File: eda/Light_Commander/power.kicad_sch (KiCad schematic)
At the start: 14 parts, among them J13 Eurorack_Power, Q5 Q_PMOS_GSD, Q6 Q_NMOS_GSD, U4 R-785.0-0.5, U5 AP2112K-3.3

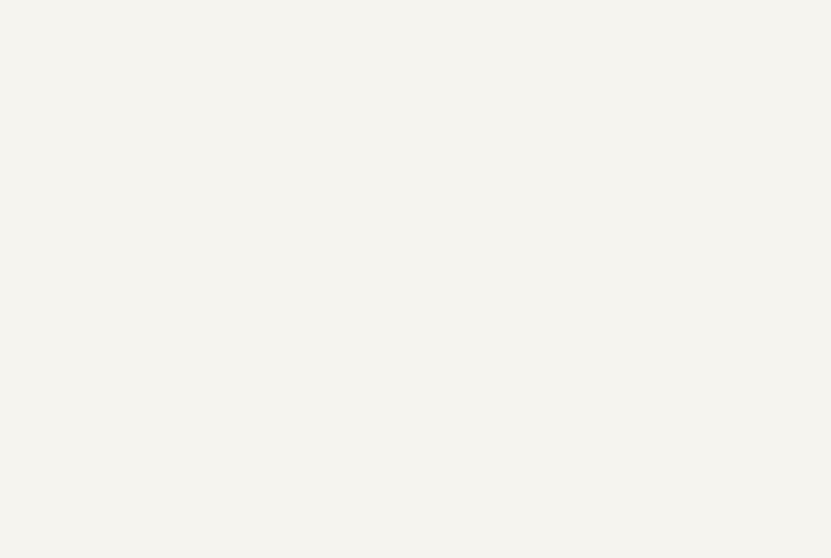
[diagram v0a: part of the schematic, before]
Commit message: Voltage ref, BOOT0, and connections on PCB
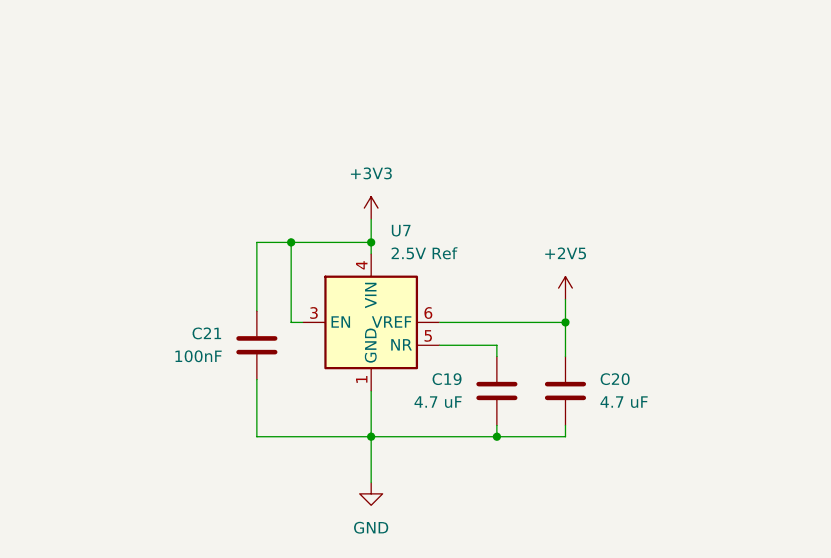
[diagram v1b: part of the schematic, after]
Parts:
- added C19, C20: 4.7 uF, Capacitor_SMD:C_0805_2012Metric, symbol Device:C
- added C21: 100nF, Capacitor_SMD:C_0805_2012Metric, symbol Device:C
- added U7: 2.5V Ref, Package_TO_SOT_SMD:SOT-23-6, symbol Reference_Voltage:REF35250QDBVR
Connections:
- net +3V3: now also C21.2, U7.3 (EN), U7.4 (VIN)
- net GND: now also C19.1, C20.1, C21.1, U7.1 (GND), U7.2 (GND)
- new net: C19.2, U7.5 (NR)
- new net +2V5: C20.2, U7.6 (VREF)
